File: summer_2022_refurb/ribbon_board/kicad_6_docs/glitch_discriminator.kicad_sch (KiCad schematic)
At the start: 17 parts

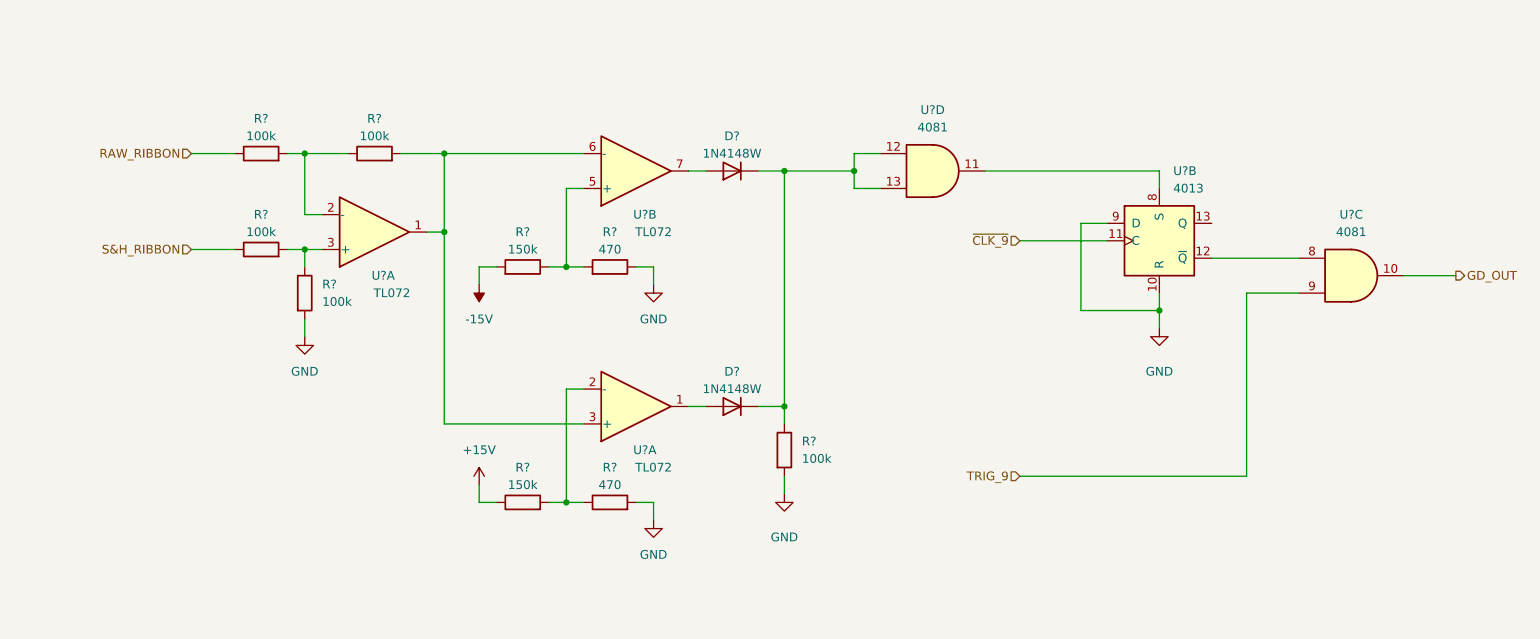
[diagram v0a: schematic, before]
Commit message: Progress on ribbon board
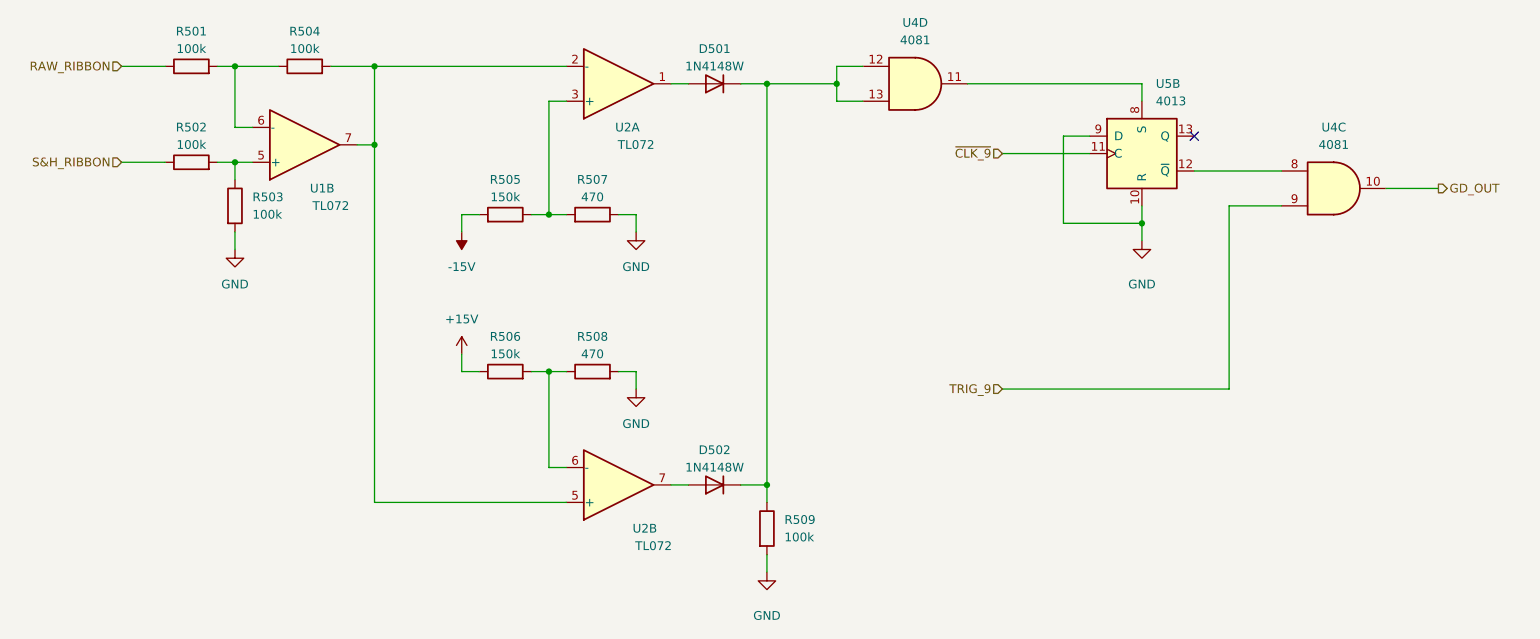
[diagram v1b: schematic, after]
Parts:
- R501, R502, R503, R504, R505, R506, R507, R508, R509: renamed from R?; footprint (none) -> Resistor_SMD:R_0805_2012Metric
- U1, U2: renamed from U?; footprint (none) -> Package_SO:SO-8_5.3x6.2mm_P1.27mm
- U4, U5: renamed from U?; footprint (none) -> Package_SO:SOIC-14_3.9x8.7mm_P1.27mm
- gave numbers to parts that had none: 2
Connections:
- net at R501.2, R504.1: now also U1.6 (-); no longer U1.2 (-)
- net at R502.2, R503.1: now also U1.5 (+); no longer U1.3 (+)
- net at R505.1, R507.2: now also U2.3 (+); no longer U2.5 (+)
- net at U2.7: now also D502.2 (A); no longer D501.2 (A)
- net at R506.2, R508.1: now also U2.6 (-); no longer U2.2 (-)
- net at U2.1: now also D501.2 (A); no longer D502.2 (A)
- new net: R504.2, U1.7, U2.2 (-), U2.5 (+)
- no-connect marks 0 -> 1
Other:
- moved on the sheet: D501, D502, R501, R502, R503, R504, R505, R506, R507, R508, R509, U1B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

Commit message: Initial ribbon board layout
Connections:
- net GD_OUT: now also U4.4; no longer U4.10
- net GND: now also U5.4 (R), U5.5 (D); no longer U5.10 (R), U5.9 (D)
- net TRIG_9: now also U4.6; no longer U4.9
- net ~{CLK_9}: now also U5.3 (C); no longer U5.11 (C)
- net at D501.1 (K), D502.1 (K), R509.1: now also U4.1, U4.2; no longer U4.12, U4.13
- new net: U4.3, U5.6 (S)
- new net: U4.5, U5.2 (~{Q})
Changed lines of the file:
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@@
     (pin "1")
   )
-  (symbol (lib_id "4xxx:4081") (at 170.18 68.58 0) (unit 4)
+  (symbol (lib_id "4xxx:4081") (at 170.18 68.58 0) (unit 1)
     (in_bom yes) (on_board yes) (fields_autoplaced)
     (property "Reference" "U4" (id 0) (at 170.18 59.69 0))
@@
     (pin "2")
   )
-  (symbol (lib_id "4xxx:4013") (at 203.2 78.74 0) (unit 2)
+  (symbol (lib_id "4xxx:4013") (at 203.2 78.74 0) (unit 1)
     (in_bom yes) (on_board yes) (fields_autoplaced)
     (property "Reference" "U5" (id 0) (at 205.2194 68.58 0)
@@
     (pin "1")
   )
-  (symbol (lib_id "4xxx:4081") (at 231.14 83.82 0) (unit 3)
+  (symbol (lib_id "4xxx:4081") (at 231.14 83.82 0) (unit 2)
     (in_bom yes) (on_board yes) (fields_autoplaced)
     (property "Reference" "U4" (id 0) (at 231.14 74.93 0))
